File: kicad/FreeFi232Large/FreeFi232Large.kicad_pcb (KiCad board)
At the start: 2 copper layers, 40.6 x 53.3 mm, 34 parts, among them J1 DB25-Female, J2 3V3-SERIAL, J3 HWFLOW, J4 USB_OTG, J5 ALT-POWER, SW1 B3S-1100, U1 MAX3237, U2 ESP-12E, U3 LM1117-3.3

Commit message: PCB to V1.1
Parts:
- added ?: VIA-0.6mm, Fiducials:VIA-0.6mm, F.Cu at (168.4, 93.2)
- added ?: VIA-0.6mm, Fiducials:VIA-0.6mm, F.Cu at (135.4, 101.6)
- added ?: VIA-0.6mm, Fiducials:VIA-0.6mm, F.Cu at (136.4, 100.1)
- added ?: VIA-0.6mm, Fiducials:VIA-0.6mm, F.Cu at (132.8, 94.7)
- added ?: VIA-0.6mm, Fiducials:VIA-0.6mm, F.Cu at (132.8, 93.0)
- added ?: VIA-0.6mm, Fiducials:VIA-0.6mm, F.Cu at (134.4, 93.0)
- added ?: VIA-0.6mm, Fiducials:VIA-0.6mm, F.Cu at (141.0, 116.1)
- added ?: VIA-0.6mm, Fiducials:VIA-0.6mm, F.Cu at (139.7, 109.0)
- added ?: VIA-0.6mm, Fiducials:VIA-0.6mm, F.Cu at (152.7, 85.9)
- added ?: VIA-0.6mm, Fiducials:VIA-0.6mm, F.Cu at (150.6, 87.9)
- added ?: VIA-0.6mm, Fiducials:VIA-0.6mm, F.Cu at (141.5, 86.1)
- added ?: VIA-0.6mm, Fiducials:VIA-0.6mm, F.Cu at (166.9, 92.2)
- added ?: VIA-0.6mm, Fiducials:VIA-0.6mm, F.Cu at (144.3, 88.4)
- added ?: VIA-0.6mm, Fiducials:VIA-0.6mm, F.Cu at (144.3, 86.4)
- added ?: VIA-0.6mm, Fiducials:VIA-0.6mm, F.Cu at (164.3, 128.3)
- added ?: VIA-0.6mm, Fiducials:VIA-0.6mm, F.Cu at (161.5, 128.3)
- added ?: VIA-0.6mm, Fiducials:VIA-0.6mm, F.Cu at (160.0, 130.8)
- added ?: VIA-0.6mm, Fiducials:VIA-0.6mm, F.Cu at (146.1, 130.8)
- added ?: VIA-0.6mm, Fiducials:VIA-0.6mm, F.Cu at (148.6, 130.8)
- added ?: VIA-0.6mm, Fiducials:VIA-0.6mm, F.Cu at (166.4, 109.2)
- added ?: VIA-0.6mm, Fiducials:VIA-0.6mm, F.Cu at (159.0, 104.1)
- added ?: VIA-0.6mm, Fiducials:VIA-0.6mm, F.Cu at (156.7, 104.1)
- added ?: VIA-0.6mm, Fiducials:VIA-0.6mm, F.Cu at (164.8, 94.7)
- added ?: VIA-0.6mm, Fiducials:VIA-0.6mm, F.Cu at (156.7, 101.6)
- added ?: VIA-0.6mm, Fiducials:VIA-0.6mm, F.Cu at (154.4, 101.6)
- added ?: VIA-0.6mm, Fiducials:VIA-0.6mm, F.Cu at (154.4, 99.1)
- added ?: VIA-0.6mm, Fiducials:VIA-0.6mm, F.Cu at (160.5, 99.1)
- added ?: VIA-0.6mm, Fiducials:VIA-0.6mm, F.Cu at (161.8, 100.3)
- added ?: VIA-0.6mm, Fiducials:VIA-0.6mm, F.Cu at (161.8, 97.8)
- added ?: VIA-0.6mm, Fiducials:VIA-0.6mm, F.Cu at (160.5, 96.5)
- added ?: VIA-0.6mm, Fiducials:VIA-0.6mm, F.Cu at (147.8, 94.0)
- added ?: VIA-0.6mm, Fiducials:VIA-0.6mm, F.Cu at (149.9, 96.5)
- added ?: VIA-0.6mm, Fiducials:VIA-0.6mm, F.Cu at (151.9, 99.1)
- added ?: VIA-0.6mm, Fiducials:VIA-0.6mm, F.Cu at (164.8, 97.3)
- added ?: VIA-0.6mm, Fiducials:VIA-0.6mm, F.Cu at (151.9, 96.5)
- added ?: VIA-0.6mm, Fiducials:VIA-0.6mm, F.Cu at (149.9, 94.0)
- added ?: VIA-0.6mm, Fiducials:VIA-0.6mm, F.Cu at (149.9, 91.4)
- added ?: VIA-0.6mm, Fiducials:VIA-0.6mm, F.Cu at (161.8, 92.7)
- added ?: VIA-0.6mm, Fiducials:VIA-0.6mm, F.Cu at (160.5, 94.0)
- added ?: VIA-0.6mm, Fiducials:VIA-0.6mm, F.Cu at (160.5, 91.4)
- added ?: VIA-0.6mm, Fiducials:VIA-0.6mm, F.Cu at (151.9, 91.4)
- added ?: VIA-0.6mm, Fiducials:VIA-0.6mm, F.Cu at (153.4, 88.9)
- added ?: VIA-0.6mm, Fiducials:VIA-0.6mm, F.Cu at (155.4, 88.9)
- added ?: VIA-0.6mm, Fiducials:VIA-0.6mm, F.Cu at (160.5, 88.9)
- added ?: VIA-0.6mm, Fiducials:VIA-0.6mm, F.Cu at (164.8, 92.2)
- added ?: VIA-0.6mm, Fiducials:VIA-0.6mm, F.Cu at (168.9, 83.8)
- added ?: VIA-0.6mm, Fiducials:VIA-0.6mm, F.Cu at (168.9, 81.5)
- added ?: VIA-0.6mm, Fiducials:VIA-0.6mm, F.Cu at (160.5, 86.4)
- added ?: VIA-0.6mm, Fiducials:VIA-0.6mm, F.Cu at (158.0, 86.4)
- added ?: VIA-0.6mm, Fiducials:VIA-0.6mm, F.Cu at (155.4, 86.4)
- added ?: VIA-0.6mm, Fiducials:VIA-0.6mm, F.Cu at (147.3, 86.4)
- added ?: VIA-0.6mm, Fiducials:VIA-0.6mm, F.Cu at (131.3, 103.1)
- added ?: VIA-0.6mm, Fiducials:VIA-0.6mm, F.Cu at (133.1, 86.4)
- added ?: VIA-0.6mm, Fiducials:VIA-0.6mm, F.Cu at (131.1, 88.9)
- added ?: VIA-0.6mm, Fiducials:VIA-0.6mm, F.Cu at (131.1, 86.4)
- added ?: VIA-0.6mm, Fiducials:VIA-0.6mm, F.Cu at (164.8, 89.7)
- added ?: VIA-0.6mm, Fiducials:VIA-0.6mm, F.Cu at (131.1, 83.8)
- added ?: VIA-0.6mm, Fiducials:VIA-0.6mm, F.Cu at (131.1, 81.3)
- added ?: VIA-0.6mm, Fiducials:VIA-0.6mm, F.Cu at (150.4, 108.0)
- added ?: VIA-0.6mm, Fiducials:VIA-0.6mm, F.Cu at (147.8, 108.0)
- added ?: VIA-0.6mm, Fiducials:VIA-0.6mm, F.Cu at (147.6, 105.2)
- added ?: VIA-0.6mm, Fiducials:VIA-0.6mm, F.Cu at (145.0, 105.2)
- added ?: VIA-0.6mm, Fiducials:VIA-0.6mm, F.Cu at (145.0, 108.0)
- added ?: VIA-0.6mm, Fiducials:VIA-0.6mm, F.Cu at (142.2, 108.0)
- added ?: VIA-0.6mm, Fiducials:VIA-0.6mm, F.Cu at (142.2, 105.2)
- added ?: VIA-0.6mm, Fiducials:VIA-0.6mm, F.Cu at (145.5, 115.6)
- added ?: VIA-0.6mm, Fiducials:VIA-0.6mm, F.Cu at (132.1, 96.8)
- added ?: VIA-0.6mm, Fiducials:VIA-0.6mm, F.Cu at (148.8, 115.6)
- added ?: VIA-0.6mm, Fiducials:VIA-0.6mm, F.Cu at (148.8, 113.3)
- added ?: VIA-0.6mm, Fiducials:VIA-0.6mm, F.Cu at (145.5, 113.3)
- added ?: VIA-0.6mm, Fiducials:VIA-0.6mm, F.Cu at (160.0, 127.0)
- added ?: VIA-0.6mm, Fiducials:VIA-0.6mm, F.Cu at (160.0, 124.5)
- added ?: VIA-0.6mm, Fiducials:VIA-0.6mm, F.Cu at (134.4, 121.9)
- added ?: VIA-0.6mm, Fiducials:VIA-0.6mm, F.Cu at (131.3, 121.9)
- added ?: VIA-0.6mm, Fiducials:VIA-0.6mm, F.Cu at (131.3, 111.8)
- added ?: VIA-0.6mm, Fiducials:VIA-0.6mm, F.Cu at (131.3, 106.7)
- added ?: VIA-0.6mm, Fiducials:VIA-0.6mm, F.Cu at (131.3, 109.2)
- added ?: VIA-0.6mm, Fiducials:VIA-0.6mm, F.Cu at (135.9, 92.2)
- added ?: VIA-0.6mm, Fiducials:VIA-0.6mm, F.Cu at (131.3, 114.3)
- added ?: VIA-0.6mm, Fiducials:VIA-0.6mm, F.Cu at (131.3, 116.8)
- added ?: VIA-0.6mm, Fiducials:VIA-0.6mm, F.Cu at (131.3, 119.4)
- added ?: VIA-0.6mm, Fiducials:VIA-0.6mm, F.Cu at (141.0, 120.7)
- added ?: VIA-0.6mm, Fiducials:VIA-0.6mm, F.Cu at (141.0, 118.1)
- added ?: VIA-0.6mm, Fiducials:VIA-0.6mm, F.Cu at (143.5, 123.2)
- added ?: VIA-0.6mm, Fiducials:VIA-0.6mm, F.Cu at (137.4, 101.6)
- moved ? 1.52 mm to (151.9, 94.0)
- moved ? 1.48 mm to (141.0, 123.2)
- moved ? 1.05 mm to (133.3, 104.1)
- moved ? 0.92 mm to (161.8, 95.2)
- moved ? 0.76 mm to (158.0, 88.9)
- moved ? 0.57 mm to (156.7, 99.1)
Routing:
- net +3V3: track 154.9 -> 122.1 mm
- net +5V: track 16.2 -> 18.2 mm

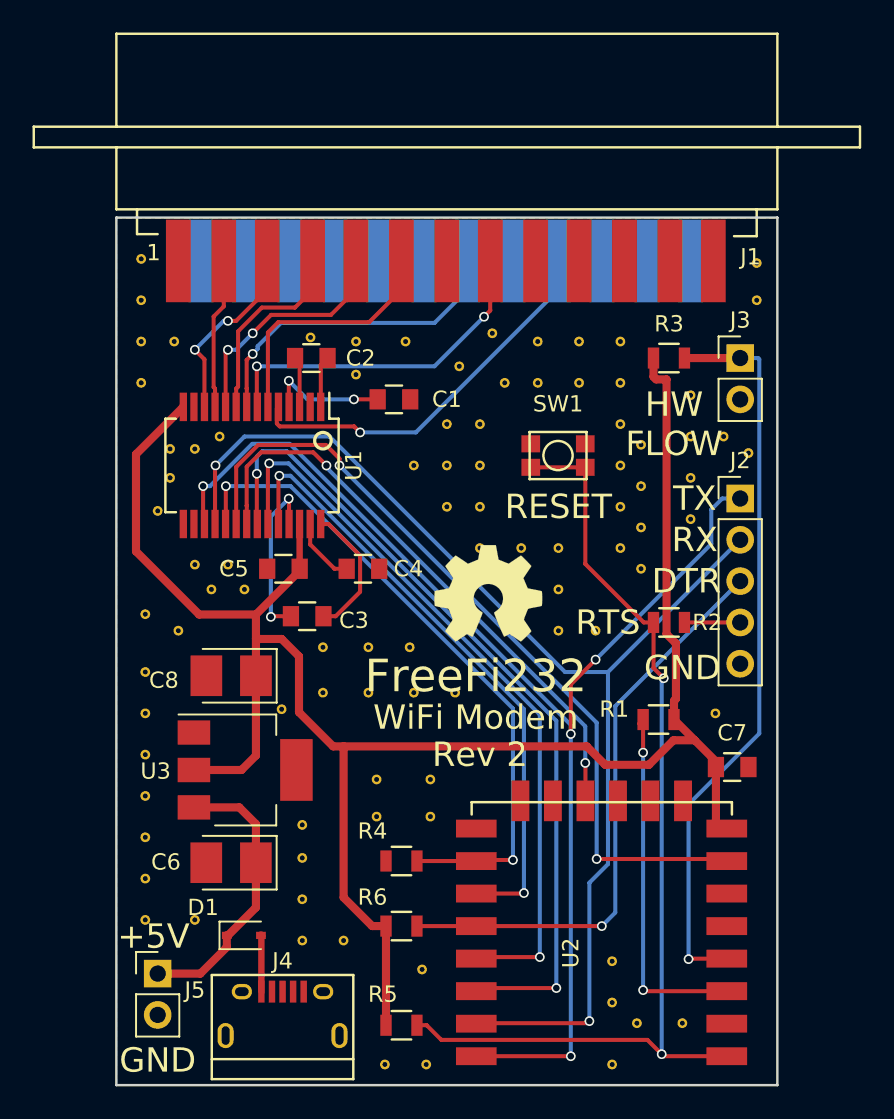
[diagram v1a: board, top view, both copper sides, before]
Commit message: Final tidying of power lines.
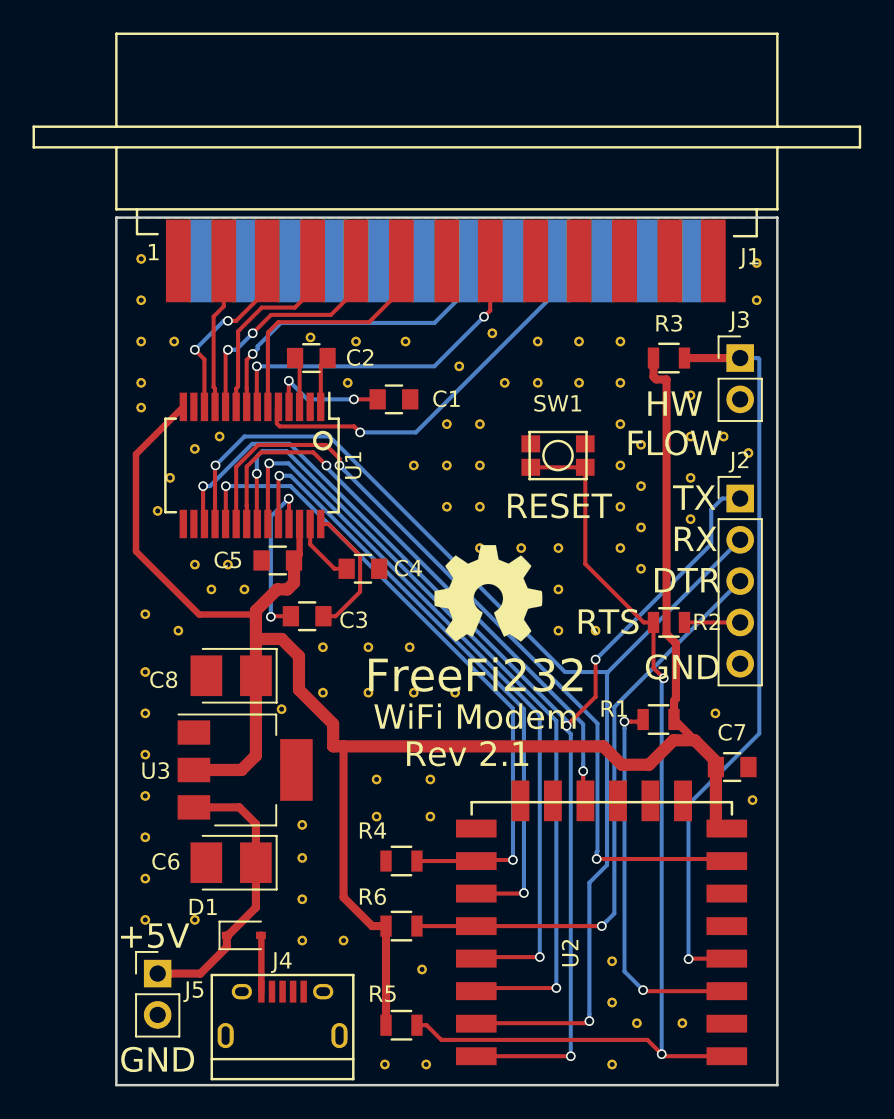
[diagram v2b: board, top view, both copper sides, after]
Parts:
- added ?: VIA-0.6mm, Fiducials:VIA-0.6mm, F.Cu at (168.7, 114.6)
- moved ? 3.10 mm to (131.1, 90.4)
- moved ? 0.72 mm to (143.8, 88.9)
- moved C5 0.62 mm to (139.5, 99.8)
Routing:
- net Net-(R1-Pad2): track 21.0 -> 22.4 mm
- net +3V3: track 122.1 -> 122.9 mm
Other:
- board text added: "Rev 2.1"
- board text removed: "Rev 2"

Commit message: Reverted to KiCAD 4.0.7, revised GPIO pins, BOM added.
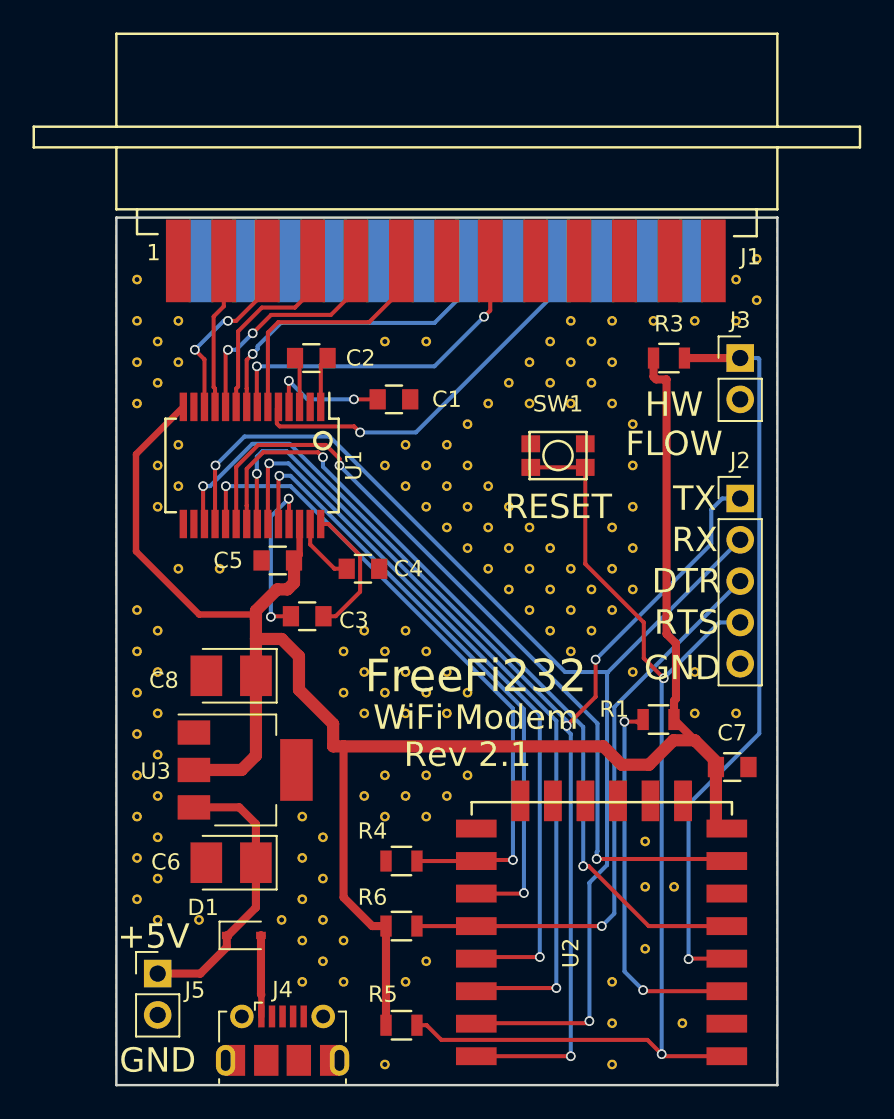
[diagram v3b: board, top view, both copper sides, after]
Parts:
- removed ? (x94): VIA-0.6mm, Fiducials:VIA-0.6mm
- removed G***: LOGO, Apple2_bus:CCBYSA
- removed R2: 470R, Resistors_SMD:R_0805
- removed REF***: OSHW-Symbol_6.7x6mm_SilkScreen, Symbols:OSHW-Symbol_6.7x6mm_SilkScreen
- added REF**: VIA-0.6mm, stitchingVIA:VIA-0.6mm, F.Cu at (141.0, 125.7)
- added REF**: VIA-0.6mm, stitchingVIA:VIA-0.6mm, F.Cu at (160.0, 128.3)
- added REF**: VIA-0.6mm, stitchingVIA:VIA-0.6mm, F.Cu at (146.1, 113.0)
- added REF**: VIA-0.6mm, stitchingVIA:VIA-0.6mm, F.Cu at (141.0, 123.2)
- added REF**: VIA-0.6mm, stitchingVIA:VIA-0.6mm, F.Cu at (143.5, 123.2)
- added REF**: VIA-0.6mm, stitchingVIA:VIA-0.6mm, F.Cu at (142.2, 121.9)
- added REF**: VIA-0.6mm, stitchingVIA:VIA-0.6mm, F.Cu at (139.7, 121.9)
- added REF**: VIA-0.6mm, stitchingVIA:VIA-0.6mm, F.Cu at (141.0, 120.7)
- added REF**: VIA-0.6mm, stitchingVIA:VIA-0.6mm, F.Cu at (142.2, 119.4)
- added REF**: VIA-0.6mm, stitchingVIA:VIA-0.6mm, F.Cu at (141.0, 118.1)
- added REF**: VIA-0.6mm, stitchingVIA:VIA-0.6mm, F.Cu at (142.2, 116.8)
- added REF**: VIA-0.6mm, stitchingVIA:VIA-0.6mm, F.Cu at (141.0, 115.6)
- added REF**: VIA-0.6mm, stitchingVIA:VIA-0.6mm, F.Cu at (160.0, 125.7)
- added REF**: VIA-0.6mm, stitchingVIA:VIA-0.6mm, F.Cu at (135.9, 100.3)
- added REF**: VIA-0.6mm, stitchingVIA:VIA-0.6mm, F.Cu at (133.3, 100.3)
- added REF**: VIA-0.6mm, stitchingVIA:VIA-0.6mm, F.Cu at (132.1, 96.5)
- added REF**: VIA-0.6mm, stitchingVIA:VIA-0.6mm, F.Cu at (133.3, 95.2)
- added REF**: VIA-0.6mm, stitchingVIA:VIA-0.6mm, F.Cu at (132.1, 94.0)
- added REF**: VIA-0.6mm, stitchingVIA:VIA-0.6mm, F.Cu at (133.3, 92.7)
- added REF**: VIA-0.6mm, stitchingVIA:VIA-0.6mm, F.Cu at (132.1, 88.9)
- added REF**: VIA-0.6mm, stitchingVIA:VIA-0.6mm, F.Cu at (130.8, 90.2)
- added REF**: VIA-0.6mm, stitchingVIA:VIA-0.6mm, F.Cu at (133.3, 85.1)
- added REF**: VIA-0.6mm, stitchingVIA:VIA-0.6mm, F.Cu at (133.3, 87.6)
- added REF**: VIA-0.6mm, stitchingVIA:VIA-0.6mm, F.Cu at (148.6, 86.4)
- added REF**: VIA-0.6mm, stitchingVIA:VIA-0.6mm, F.Cu at (132.1, 86.4)
- added REF**: VIA-0.6mm, stitchingVIA:VIA-0.6mm, F.Cu at (134.6, 121.9)
- added REF**: VIA-0.6mm, stitchingVIA:VIA-0.6mm, F.Cu at (132.1, 121.9)
- added REF**: VIA-0.6mm, stitchingVIA:VIA-0.6mm, F.Cu at (130.8, 120.7)
- added REF**: VIA-0.6mm, stitchingVIA:VIA-0.6mm, F.Cu at (132.1, 119.4)
- added REF**: VIA-0.6mm, stitchingVIA:VIA-0.6mm, F.Cu at (130.8, 118.1)
- added REF**: VIA-0.6mm, stitchingVIA:VIA-0.6mm, F.Cu at (132.1, 116.8)
- added REF**: VIA-0.6mm, stitchingVIA:VIA-0.6mm, F.Cu at (130.8, 115.6)
- added REF**: VIA-0.6mm, stitchingVIA:VIA-0.6mm, F.Cu at (132.1, 114.3)
- added REF**: VIA-0.6mm, stitchingVIA:VIA-0.6mm, F.Cu at (130.8, 113.0)
- added REF**: VIA-0.6mm, stitchingVIA:VIA-0.6mm, F.Cu at (146.1, 86.4)
- added REF**: VIA-0.6mm, stitchingVIA:VIA-0.6mm, F.Cu at (132.1, 111.8)
- added REF**: VIA-0.6mm, stitchingVIA:VIA-0.6mm, F.Cu at (130.8, 110.5)
- added REF**: VIA-0.6mm, stitchingVIA:VIA-0.6mm, F.Cu at (132.1, 109.2)
- added REF**: VIA-0.6mm, stitchingVIA:VIA-0.6mm, F.Cu at (130.8, 108.0)
- added REF**: VIA-0.6mm, stitchingVIA:VIA-0.6mm, F.Cu at (132.1, 106.7)
- added REF**: VIA-0.6mm, stitchingVIA:VIA-0.6mm, F.Cu at (130.8, 105.4)
- added REF**: VIA-0.6mm, stitchingVIA:VIA-0.6mm, F.Cu at (132.1, 104.1)
- added REF**: VIA-0.6mm, stitchingVIA:VIA-0.6mm, F.Cu at (130.8, 102.9)
- added REF**: VIA-0.6mm, stitchingVIA:VIA-0.6mm, F.Cu at (130.8, 87.6)
- added REF**: VIA-0.6mm, stitchingVIA:VIA-0.6mm, F.Cu at (130.8, 85.1)
- added REF**: VIA-0.6mm, stitchingVIA:VIA-0.6mm, F.Cu at (167.6, 109.2)
- added REF**: VIA-0.6mm, stitchingVIA:VIA-0.6mm, F.Cu at (130.8, 82.5)
- added REF**: VIA-0.6mm, stitchingVIA:VIA-0.6mm, F.Cu at (165.1, 109.2)
- added REF**: VIA-0.6mm, stitchingVIA:VIA-0.6mm, F.Cu at (165.1, 106.7)
- added REF**: VIA-0.6mm, stitchingVIA:VIA-0.6mm, F.Cu at (161.3, 106.7)
- added REF**: VIA-0.6mm, stitchingVIA:VIA-0.6mm, F.Cu at (160.0, 102.9)
- added REF**: VIA-0.6mm, stitchingVIA:VIA-0.6mm, F.Cu at (158.8, 101.6)
- added REF**: VIA-0.6mm, stitchingVIA:VIA-0.6mm, F.Cu at (143.5, 125.7)
- added REF**: VIA-0.6mm, stitchingVIA:VIA-0.6mm, F.Cu at (158.8, 104.1)
- added REF**: VIA-0.6mm, stitchingVIA:VIA-0.6mm, F.Cu at (160.0, 100.3)
- added REF**: VIA-0.6mm, stitchingVIA:VIA-0.6mm, F.Cu at (161.3, 101.6)
- added REF**: VIA-0.6mm, stitchingVIA:VIA-0.6mm, F.Cu at (160.0, 97.8)
- added REF**: VIA-0.6mm, stitchingVIA:VIA-0.6mm, F.Cu at (161.3, 99.1)
- added REF**: VIA-0.6mm, stitchingVIA:VIA-0.6mm, F.Cu at (161.3, 96.5)
- added REF**: VIA-0.6mm, stitchingVIA:VIA-0.6mm, F.Cu at (161.3, 94.0)
- added REF**: VIA-0.6mm, stitchingVIA:VIA-0.6mm, F.Cu at (161.3, 91.4)
- added REF**: VIA-0.6mm, stitchingVIA:VIA-0.6mm, F.Cu at (160.0, 90.2)
- added REF**: VIA-0.6mm, stitchingVIA:VIA-0.6mm, F.Cu at (160.0, 87.6)
- added REF**: VIA-0.6mm, stitchingVIA:VIA-0.6mm, F.Cu at (142.2, 124.5)
- added REF**: VIA-0.6mm, stitchingVIA:VIA-0.6mm, F.Cu at (158.8, 88.9)
- added REF**: VIA-0.6mm, stitchingVIA:VIA-0.6mm, F.Cu at (157.5, 90.2)
- added REF**: VIA-0.6mm, stitchingVIA:VIA-0.6mm, F.Cu at (154.9, 90.2)
- added REF**: VIA-0.6mm, stitchingVIA:VIA-0.6mm, F.Cu at (156.2, 88.9)
- added REF**: VIA-0.6mm, stitchingVIA:VIA-0.6mm, F.Cu at (157.5, 87.6)
- added REF**: VIA-0.6mm, stitchingVIA:VIA-0.6mm, F.Cu at (168.9, 81.3)
- added REF**: VIA-0.6mm, stitchingVIA:VIA-0.6mm, F.Cu at (167.6, 82.5)
- added REF**: VIA-0.6mm, stitchingVIA:VIA-0.6mm, F.Cu at (168.9, 83.8)
- added REF**: VIA-0.6mm, stitchingVIA:VIA-0.6mm, F.Cu at (167.6, 85.1)
- added REF**: VIA-0.6mm, stitchingVIA:VIA-0.6mm, F.Cu at (165.1, 85.1)
- added REF**: VIA-0.6mm, stitchingVIA:VIA-0.6mm, F.Cu at (160.0, 130.8)
- added REF**: VIA-0.6mm, stitchingVIA:VIA-0.6mm, F.Cu at (162.6, 85.1)
- added REF**: VIA-0.6mm, stitchingVIA:VIA-0.6mm, F.Cu at (160.0, 85.1)
- added REF**: VIA-0.6mm, stitchingVIA:VIA-0.6mm, F.Cu at (158.8, 86.4)
- added REF**: VIA-0.6mm, stitchingVIA:VIA-0.6mm, F.Cu at (157.5, 85.1)
- added REF**: VIA-0.6mm, stitchingVIA:VIA-0.6mm, F.Cu at (156.2, 86.4)
- added REF**: VIA-0.6mm, stitchingVIA:VIA-0.6mm, F.Cu at (154.9, 87.6)
- added REF**: VIA-0.6mm, stitchingVIA:VIA-0.6mm, F.Cu at (153.7, 88.9)
- added REF**: VIA-0.6mm, stitchingVIA:VIA-0.6mm, F.Cu at (152.4, 90.2)
- added REF**: VIA-0.6mm, stitchingVIA:VIA-0.6mm, F.Cu at (151.1, 91.4)
- added REF**: VIA-0.6mm, stitchingVIA:VIA-0.6mm, F.Cu at (157.5, 100.3)
- added REF**: VIA-0.6mm, stitchingVIA:VIA-0.6mm, F.Cu at (162.1, 117.1)
- added REF**: VIA-0.6mm, stitchingVIA:VIA-0.6mm, F.Cu at (156.2, 99.1)
- added REF**: VIA-0.6mm, stitchingVIA:VIA-0.6mm, F.Cu at (154.9, 97.8)
- added REF**: VIA-0.6mm, stitchingVIA:VIA-0.6mm, F.Cu at (153.7, 96.5)
- added REF**: VIA-0.6mm, stitchingVIA:VIA-0.6mm, F.Cu at (152.4, 95.2)
- added REF**: VIA-0.6mm, stitchingVIA:VIA-0.6mm, F.Cu at (151.1, 94.0)
- added REF**: VIA-0.6mm, stitchingVIA:VIA-0.6mm, F.Cu at (149.9, 92.7)
- added REF**: VIA-0.6mm, stitchingVIA:VIA-0.6mm, F.Cu at (149.9, 95.2)
- added REF**: VIA-0.6mm, stitchingVIA:VIA-0.6mm, F.Cu at (151.1, 96.5)
- added REF**: VIA-0.6mm, stitchingVIA:VIA-0.6mm, F.Cu at (152.4, 97.8)
- added REF**: VIA-0.6mm, stitchingVIA:VIA-0.6mm, F.Cu at (153.7, 99.1)
- added REF**: VIA-0.6mm, stitchingVIA:VIA-0.6mm, F.Cu at (163.8, 119.9)
- added REF**: VIA-0.6mm, stitchingVIA:VIA-0.6mm, F.Cu at (154.9, 100.3)
- added REF**: VIA-0.6mm, stitchingVIA:VIA-0.6mm, F.Cu at (156.2, 101.6)
- added REF**: VIA-0.6mm, stitchingVIA:VIA-0.6mm, F.Cu at (157.5, 102.9)
- added REF**: VIA-0.6mm, stitchingVIA:VIA-0.6mm, F.Cu at (157.5, 105.4)
- added REF**: VIA-0.6mm, stitchingVIA:VIA-0.6mm, F.Cu at (156.2, 104.1)
- added REF**: VIA-0.6mm, stitchingVIA:VIA-0.6mm, F.Cu at (154.9, 102.9)
- added REF**: VIA-0.6mm, stitchingVIA:VIA-0.6mm, F.Cu at (153.7, 101.6)
- added REF**: VIA-0.6mm, stitchingVIA:VIA-0.6mm, F.Cu at (152.4, 100.3)
- added REF**: VIA-0.6mm, stitchingVIA:VIA-0.6mm, F.Cu at (151.1, 99.1)
- added REF**: VIA-0.6mm, stitchingVIA:VIA-0.6mm, F.Cu at (149.9, 97.8)
- added REF**: VIA-0.6mm, stitchingVIA:VIA-0.6mm, F.Cu at (162.1, 119.9)
- added REF**: VIA-0.6mm, stitchingVIA:VIA-0.6mm, F.Cu at (148.6, 96.5)
- added REF**: VIA-0.6mm, stitchingVIA:VIA-0.6mm, F.Cu at (148.6, 94.0)
- added REF**: VIA-0.6mm, stitchingVIA:VIA-0.6mm, F.Cu at (147.3, 95.2)
- added REF**: VIA-0.6mm, stitchingVIA:VIA-0.6mm, F.Cu at (147.3, 92.7)
- added REF**: VIA-0.6mm, stitchingVIA:VIA-0.6mm, F.Cu at (146.1, 94.0)
- added REF**: VIA-0.6mm, stitchingVIA:VIA-0.6mm, F.Cu at (151.1, 108.0)
- added REF**: VIA-0.6mm, stitchingVIA:VIA-0.6mm, F.Cu at (149.9, 106.7)
- added REF**: VIA-0.6mm, stitchingVIA:VIA-0.6mm, F.Cu at (149.9, 109.2)
- added REF**: VIA-0.6mm, stitchingVIA:VIA-0.6mm, F.Cu at (147.3, 109.2)
- added REF**: VIA-0.6mm, stitchingVIA:VIA-0.6mm, F.Cu at (148.6, 108.0)
- added REF**: VIA-0.6mm, stitchingVIA:VIA-0.6mm, F.Cu at (164.3, 128.3)
- added REF**: VIA-0.6mm, stitchingVIA:VIA-0.6mm, F.Cu at (147.3, 106.7)
- added REF**: VIA-0.6mm, stitchingVIA:VIA-0.6mm, F.Cu at (148.6, 105.4)
- added REF**: VIA-0.6mm, stitchingVIA:VIA-0.6mm, F.Cu at (147.3, 104.1)
- added REF**: VIA-0.6mm, stitchingVIA:VIA-0.6mm, F.Cu at (146.1, 108.0)
- added REF**: VIA-0.6mm, stitchingVIA:VIA-0.6mm, F.Cu at (146.1, 105.4)
- added REF**: VIA-0.6mm, stitchingVIA:VIA-0.6mm, F.Cu at (144.8, 104.1)
- added REF**: VIA-0.6mm, stitchingVIA:VIA-0.6mm, F.Cu at (143.5, 105.4)
- added REF**: VIA-0.6mm, stitchingVIA:VIA-0.6mm, F.Cu at (144.8, 106.7)
- added REF**: VIA-0.6mm, stitchingVIA:VIA-0.6mm, F.Cu at (143.5, 108.0)
- added REF**: VIA-0.6mm, stitchingVIA:VIA-0.6mm, F.Cu at (144.8, 109.2)
- added REF**: VIA-0.6mm, stitchingVIA:VIA-0.6mm, F.Cu at (162.1, 123.7)
- added REF**: VIA-0.6mm, stitchingVIA:VIA-0.6mm, F.Cu at (146.1, 130.8)
- added REF**: VIA-0.6mm, stitchingVIA:VIA-0.6mm, F.Cu at (147.3, 125.7)
- added REF**: VIA-0.6mm, stitchingVIA:VIA-0.6mm, F.Cu at (148.6, 124.5)
- added REF**: VIA-0.6mm, stitchingVIA:VIA-0.6mm, F.Cu at (151.1, 113.0)
- added REF**: VIA-0.6mm, stitchingVIA:VIA-0.6mm, F.Cu at (149.9, 114.3)
- added REF**: VIA-0.6mm, stitchingVIA:VIA-0.6mm, F.Cu at (148.6, 113.0)
- added REF**: VIA-0.6mm, stitchingVIA:VIA-0.6mm, F.Cu at (148.6, 115.6)
- added REF**: VIA-0.6mm, stitchingVIA:VIA-0.6mm, F.Cu at (146.1, 115.6)
- added REF**: VIA-0.6mm, stitchingVIA:VIA-0.6mm, F.Cu at (147.3, 114.3)
- added REF**: VIA-0.6mm, stitchingVIA:VIA-0.6mm, F.Cu at (144.8, 114.3)
- J4: footprint Connectors:USB_Micro-B -> Connectors_USB:USB_Micro-B_Molex-105017-0001
- moved J4 2.31 mm to (139.8, 130.2)
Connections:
- J1 pad 10: (no net) -> Net-(J1-Pad10)
- J1 pad 11: (no net) -> Net-(J1-Pad11)
- J1 pad 12: (no net) -> Net-(J1-Pad12)
- J1 pad 13: (no net) -> Net-(J1-Pad13)
- J1 pad 14: (no net) -> Net-(J1-Pad14)
- J1 pad 15: (no net) -> Net-(J1-Pad15)
- J1 pad 16: (no net) -> Net-(J1-Pad16)
- J1 pad 17: (no net) -> Net-(J1-Pad17)
- J1 pad 18: (no net) -> Net-(J1-Pad18)
- J1 pad 19: (no net) -> Net-(J1-Pad19)
- J1 pad 21: (no net) -> Net-(J1-Pad21)
- J1 pad 23: (no net) -> Net-(J1-Pad23)
- J1 pad 24: (no net) -> Net-(J1-Pad24)
- J1 pad 25: (no net) -> Net-(J1-Pad25)
- J1 pad 9: (no net) -> Net-(J1-Pad9)
- J2 pad 4: Net-(J2-Pad4) -> RESET
- J4 pad 2: (no net) -> Net-(J4-Pad2)
- J4 pad 3: (no net) -> Net-(J4-Pad3)
- J4 pad 4: (no net) -> Net-(J4-Pad4)
- U1 pad 16: (no net) -> Net-(U1-Pad16)
- U1 pad 21: GPIO10 -> GPIO14
- U2 pad 17: (no net) -> Net-(U2-Pad17)
- U2 pad 18: (no net) -> Net-(U2-Pad18)
- U2 pad 19: (no net) -> Net-(U2-Pad19)
- U2 pad 2: (no net) -> Net-(U2-Pad2)
- U2 pad 20: GPIO10 -> Net-(U2-Pad20)
- U2 pad 21: (no net) -> Net-(U2-Pad21)
- U2 pad 22: (no net) -> Net-(U2-Pad22)
- U2 pad 5: (no net) -> GPIO14
- U2 pad 6: (no net) -> Net-(U2-Pad6)
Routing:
- net GPIO14: track 0.00 -> 50.1 mm, vias 0 -> 2
- net GPIO10: track 38.8 -> 0.00 mm, vias 2 -> 0
- net RESET: track 61.2 -> 66.7 mm
- net Net-(J2-Pad4): track 3.43 -> 0.00 mm
- net Net-(U2-Pad20): track 0.00 -> 1.95 mm
- net Net-(D1-Pad2): track 3.47 -> 5.03 mm

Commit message: updated silkscreen
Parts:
- added G***: LOGO, LOGO, B.Cu at (149.9, 105.4)
- added REF***: OSHW-Logo2_7.3x6mm_SilkScreen, Symbols:OSHW-Logo2_7.3x6mm_SilkScreen, F.Cu at (151.1, 101.3)
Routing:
- net RXD0: track 74.2 -> 75.2 mm
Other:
- board text added: "Rev 2.2"
- board text removed: "Rev 2.1"
